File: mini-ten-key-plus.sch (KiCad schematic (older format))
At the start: 45 parts, among them SW0 SW_Push, U0 ProMicro

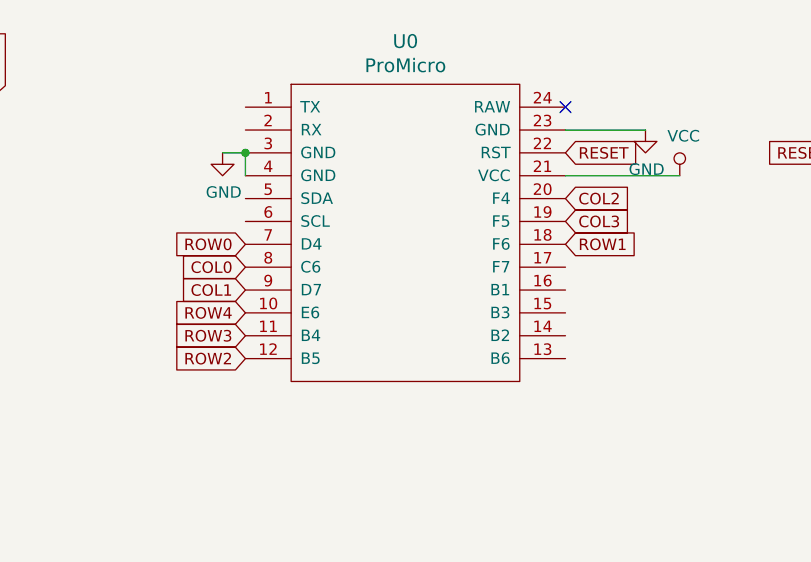
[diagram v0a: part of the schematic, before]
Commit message: Flipped Pro Micro and redid rows/cols
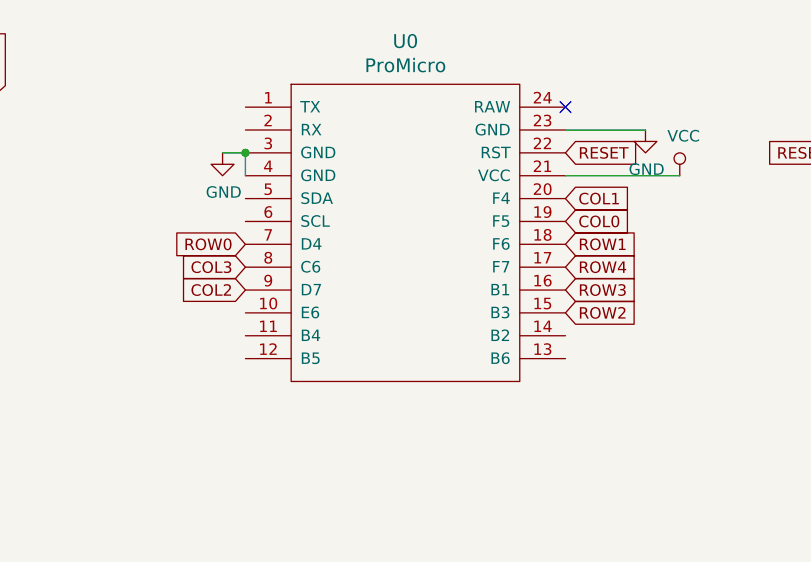
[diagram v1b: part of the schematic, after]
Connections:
- net COL0: now also U0.19 (F5); no longer U0.8 (C6)
- net COL1: now also U0.20 (F4); no longer U0.9 (D7)
- net COL2: now also U0.9 (D7); no longer U0.20 (F4)
- net COL3: now also U0.8 (C6); no longer U0.19 (F5)
- net ROW2: now also U0.15 (B3); no longer U0.12 (B5)
- net ROW3: now also U0.16 (B1); no longer U0.11 (B4)
- net ROW4: now also U0.17 (F7); no longer U0.10 (E6)
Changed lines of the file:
@@
 	1    0    0    -1
 $EndComp
+Text GLabel 3650 1550 0    50   Input ~ 0
+COL3
 Text GLabel 5050 1350 2    50   Input ~ 0
-COL3
-Text GLabel 3650 1550 0    50   Input ~ 0
 COL0
 Text GLabel 5050 1450 2    50   Input ~ 0
@@
 Text GLabel 3650 1450 0    50   Input ~ 0
 ROW0
-Text GLabel 3650 1950 0    50   Input ~ 0
+Text GLabel 5050 1750 2    50   Input ~ 0
 ROW2
-Text GLabel 3650 1750 0    50   Input ~ 0
+Text GLabel 5050 1550 2    50   Input ~ 0
 ROW4
-Text GLabel 3650 1850 0    50   Input ~ 0
+Text GLabel 5050 1650 2    50   Input ~ 0
 ROW3
+Text GLabel 5050 1250 2    50   Input ~ 0
+COL1
 Text GLabel 3650 1650 0    50   Input ~ 0
-COL1
-Text GLabel 5050 1250 2    50   Input ~ 0
 COL2
 $EndSCHEMATC

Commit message: General routing
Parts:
- added H0, H1, H2, H3, H4: MountingHole_Pad, mini-general-tweaks:MountingHole_2.2mm_M2_Pad_tweaked, symbol Mechanical:MountingHole_Pad
- MX21: footprint mini-MX-Tweaks:MXOnly-2U-NoLED_tweak -> mini-MX-Tweaks:MXOnly-2U-NoLED_FLIPPED_tweak
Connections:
- net GND: now also H0.1, H1.1, H2.1, H3.1, H4.1
- net ROW1: now also U0.16 (B1); no longer U0.18 (F6)
- net ROW2: now also U0.12 (B5); no longer U0.15 (B3)
- net ROW3: now also U0.11 (B4); no longer U0.16 (B1)
- net ROW4: now also U0.10 (E6); no longer U0.17 (F7)
- no-connect marks 1 -> 7
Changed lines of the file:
@@
 F 0 "MX21" H 1324 3973 60  0000 C CNN
 F 1 "MX-NoLED" H 1324 3899 20  0000 C CNN
-F 2 "mini-MX-Tweaks:MXOnly-2U-NoLED_tweak" H 725 3725 60  0001 C CNN
+F 2 "mini-MX-Tweaks:MXOnly-2U-NoLED_FLIPPED_tweak" H 725 3725 60  0001 C CNN
 F 3 "" H 725 3725 60  0001 C CNN
 	1    1350 3750
@@
 Text GLabel 5050 1350 2    50   Input ~ 0
 COL0
-Text GLabel 5050 1450 2    50   Input ~ 0
+Text GLabel 5050 1650 2    50   Input ~ 0
 ROW1
 Text GLabel 3650 1450 0    50   Input ~ 0
 ROW0
-Text GLabel 5050 1750 2    50   Input ~ 0
+Text GLabel 3650 1950 0    50   Input ~ 0
 ROW2
-Text GLabel 5050 1550 2    50   Input ~ 0
+Text GLabel 3650 1750 0    50   Input ~ 0
 ROW4
-Text GLabel 5050 1650 2    50   Input ~ 0
+Text GLabel 3650 1850 0    50   Input ~ 0
 ROW3
 Text GLabel 5050 1250 2    50   Input ~ 0
@@
 Text GLabel 3650 1650 0    50   Input ~ 0
 COL2
+NoConn ~ 3650 850
+NoConn ~ 3650 950
+NoConn ~ 3650 1250
+NoConn ~ 3650 1350
+NoConn ~ 5050 1850
+NoConn ~ 5050 1950
+$Comp
+L Mechanical:MountingHole_Pad H0
+U 1 1 617941C0
+P 3650 2550
+F 0 "H0" H 3750 2599 50  0000 L CNN
+F 1 "MountingHole_Pad" H 3750 2508 50  0000 L CNN
+F 2 "mini-general-tweaks:MountingHole_2.2mm_M2_Pad_tweaked" H 3650 2550 50  0001 C CNN
+F 3 "~" H 3650 2550 50  0001 C CNN
+	1    3650 2550
+	1    0    0    -1
+$EndComp
+$Comp
+L Mechanical:MountingHole_Pad H1
+U 1 1 61795197
+P 3650 2850
+F 0 "H1" H 3750 2899 50  0000 L CNN
+F 1 "MountingHole_Pad" H 3750 2808 50  0000 L CNN
+F 2 "mini-general-tweaks:MountingHole_2.2mm_M2_Pad_tweaked" H 3650 2850 50  0001 C CNN
+F 3 "~" H 3650 2850 50  0001 C CNN
+	1    3650 2850
+	1    0    0    -1
+$EndComp
+$Comp
+L Mechanical:MountingHole_Pad H2
+U 1 1 6179748B
+P 3650 3150
+F 0 "H2" H 3750 3199 50  0000 L CNN
+F 1 "MountingHole_Pad" H 3750 3108 50  0000 L CNN
+F 2 "mini-general-tweaks:MountingHole_2.2mm_M2_Pad_tweaked" H 3650 3150 50  0001 C CNN
+F 3 "~" H 3650 3150 50  0001 C CNN
+	1    3650 3150
+	1    0    0    -1
+$EndComp
+$Comp
+L Mechanical:MountingHole_Pad H3
+U 1 1 617998EF
+P 3650 3450
+F 0 "H3" H 3750 3499 50  0000 L CNN
+F 1 "MountingHole_Pad" H 3750 3408 50  0000 L CNN
+F 2 "mini-general-tweaks:MountingHole_2.2mm_M2_Pad_tweaked" H 3650 3450 50  0001 C CNN
+F 3 "~" H 3650 3450 50  0001 C CNN
+	1    3650 3450
+	1    0    0    -1
+$EndComp
+Wire Wire Line
+	3650 2650 3500 2650
+Wire Wire Line
+	3500 2650 3500 2950
+Wire Wire Line
+	3650 3550 3500 3550
+Wire Wire Line
+	3650 3250 3500 3250
+Connection ~ 3500 3250
+Wire Wire Line
+	3500 3250 3500 3550
+Wire Wire Line
+	3650 2950 3500 2950
+Connection ~ 3500 2950
+Wire Wire Line
+	3500 2950 3500 3250
+$Comp
+L power:GND #PWR0105
+U 1 1 617A50D9
+P 3500 3850
+F 0 "#PWR0105" H 3500 3600 50  0001 C CNN
+F 1 "GND" H 3505 3677 50  0000 C CNN
+F 2 "" H 3500 3850 50  0001 C CNN
+F 3 "" H 3500 3850 50  0001 C CNN
+	1    3500 3850
+	1    0    0    -1
+$EndComp
+$Comp
+L Mechanical:MountingHole_Pad H4
+U 1 1 617BCB5D
+P 3650 3750
+F 0 "H4" H 3750 3799 50  0000 L CNN
+F 1 "MountingHole_Pad" H 3750 3708 50  0000 L CNN
+F 2 "mini-general-tweaks:MountingHole_2.2mm_M2_Pad_tweaked" H 3650 3750 50  0001 C CNN
+F 3 "~" H 3650 3750 50  0001 C CNN
+	1    3650 3750
+	1    0    0    -1
+$EndComp
+Wire Wire Line
+	3500 3550 3500 3850
+Wire Wire Line
+	3500 3850 3650 3850
+Connection ~ 3500 3550
+Connection ~ 3500 3850
 $EndSCHEMATC

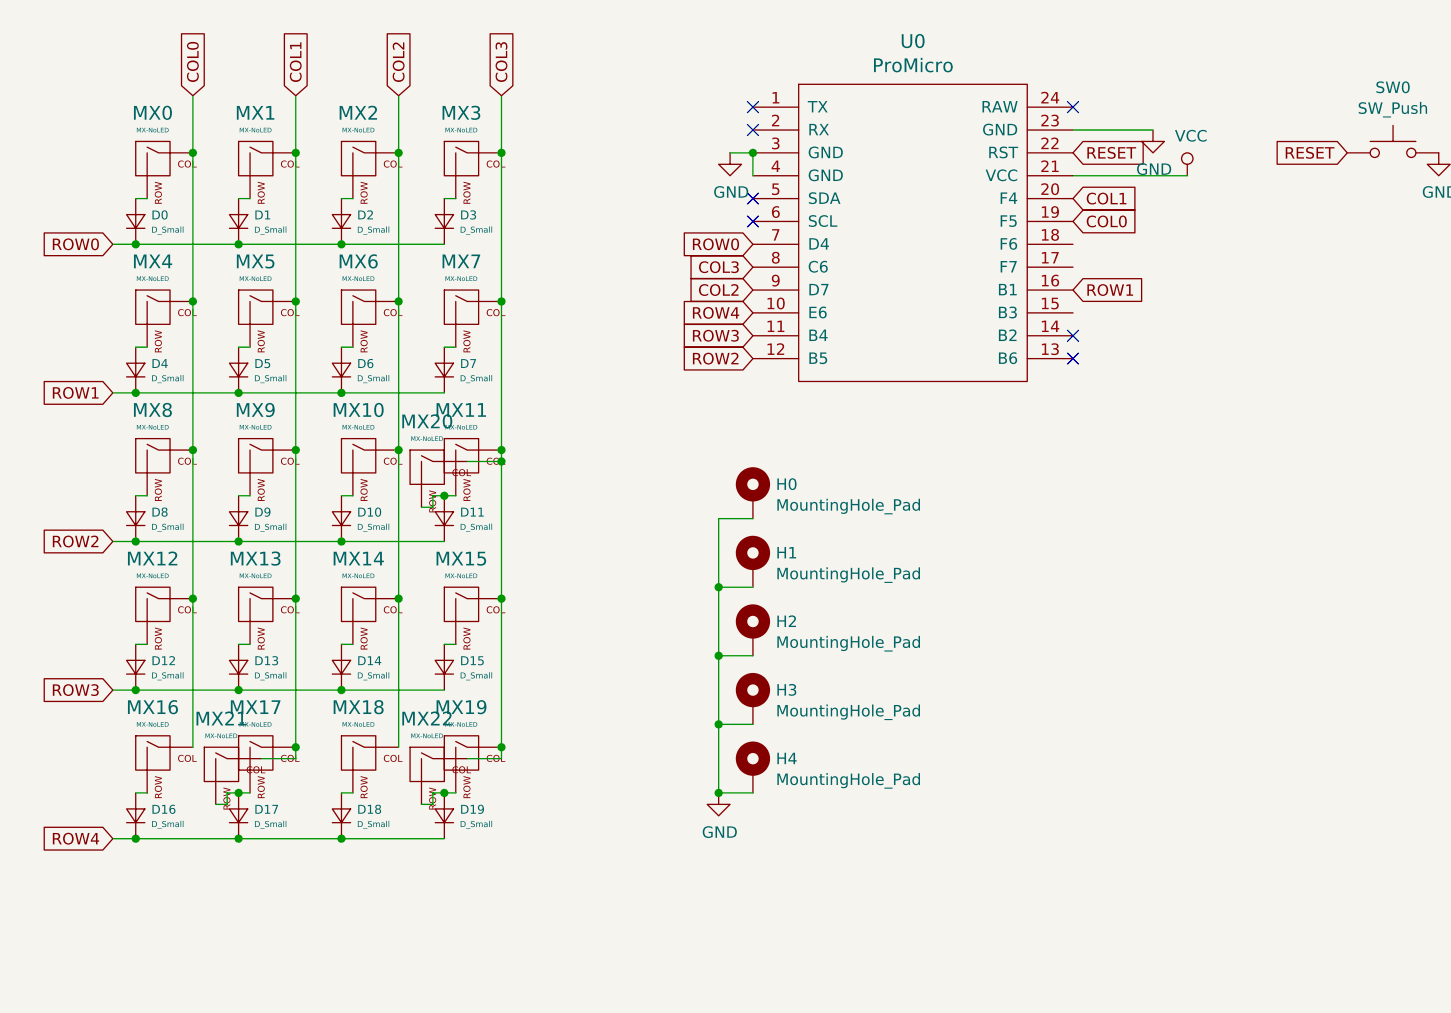
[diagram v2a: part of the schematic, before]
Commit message: Added extra column of keys on the left side
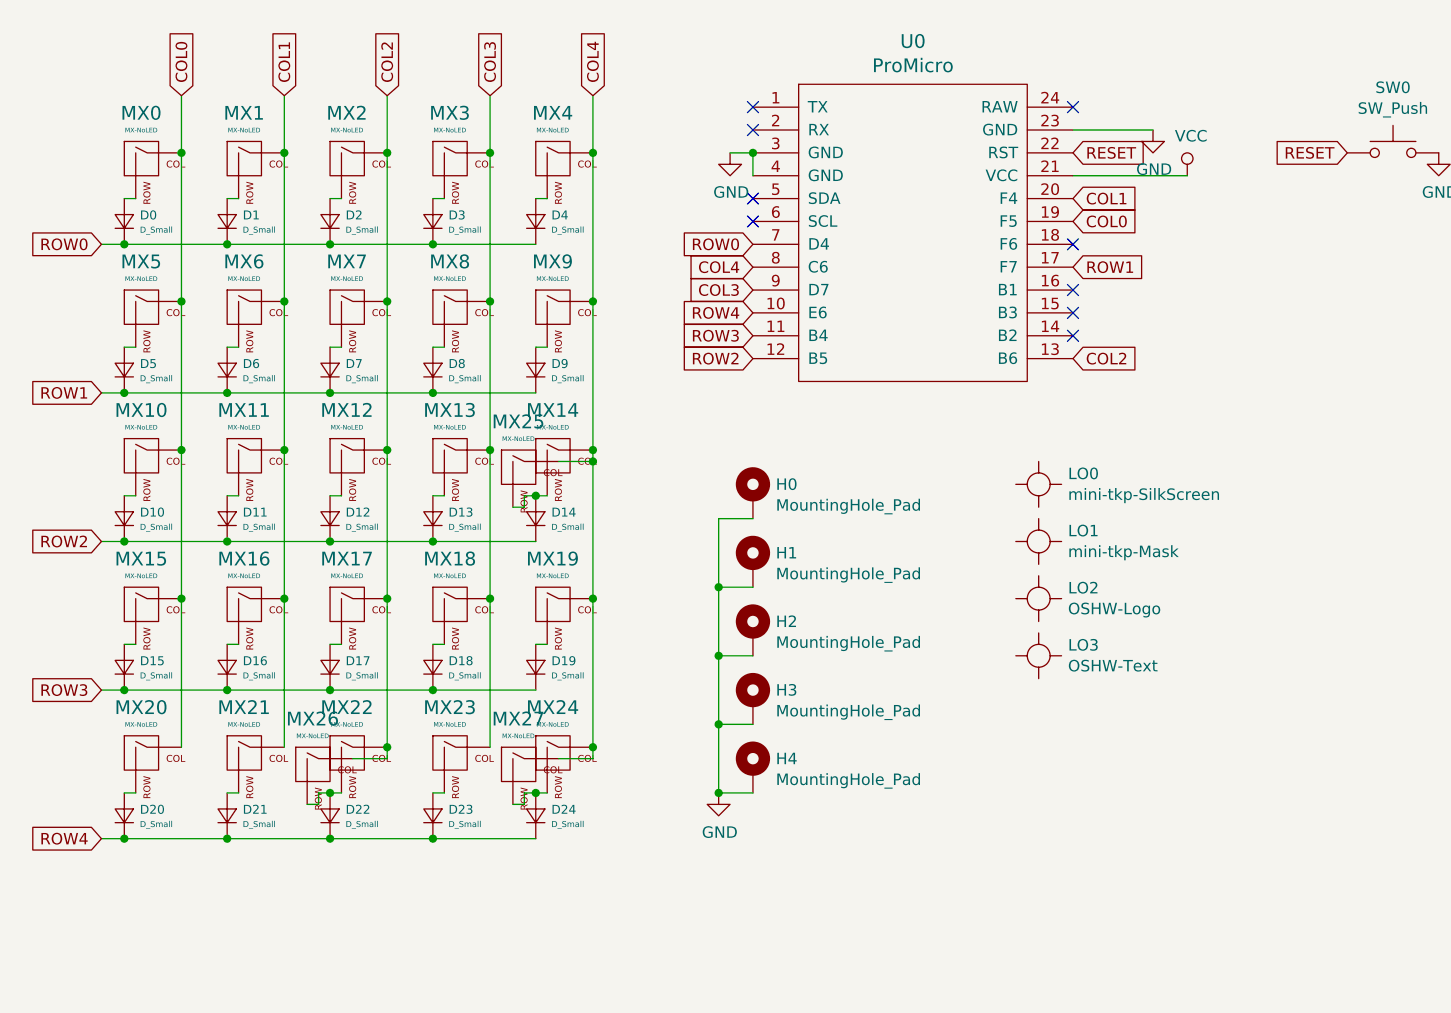
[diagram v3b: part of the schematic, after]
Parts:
- added D0, D10, D15, D20, D5: D_Small, mini-general-tweaks:D_SOD123_axial-dual, symbol Device:D_Small
- added LO0: mini-tkp-SilkScreen, mini-Logos:eLiXiVy-rev1.1-SilkScreen, symbol mini_random_library:Logo
- added LO1: mini-tkp-Mask, mini-Logos:eLiXiVy-rev1.1-Mask, symbol mini_random_library:Logo
- added LO2: OSHW-Logo, mini-Logos:OSHW-Logo, symbol mini_random_library:Logo
- added LO3: OSHW-Text, mini-Logos:OSHW-Text, symbol mini_random_library:Logo
- added MX0, MX10, MX15, MX20, MX5: MX-NoLED, mini-MX-Tweaks:MXOnly-1U-NoLED_tweak, symbol MX_Alps_Hybrid:MX-NoLED
- renumbered D0 to D1, D8 to D11, D9 to D12, D10 to D13, D11 to D14, D12 to D16, D13 to D17, D14 to D18, D15 to D19, D1 to D2, D16 to D21, D17 to D22, D18 to D23, D19 to D24, D2 to D3, D3 to D4, D4 to D6, D5 to D7, D6 to D8, D7 to D9, MX0 to MX1, MX8 to MX11, MX9 to MX12, MX10 to MX13, MX11 to MX14, MX12 to MX16, MX13 to MX17, MX14 to MX18, MX15 to MX19, MX1 to MX2, MX16 to MX21, MX17 to MX22, MX18 to MX23, MX19 to MX24, MX20 to MX25, MX21 to MX26, MX22 to MX27, MX2 to MX3, MX3 to MX4, MX4 to MX6, MX5 to MX7, MX6 to MX8, MX7 to MX9
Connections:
- net COL0: now also MX0.1 (COL), MX10.1 (COL), MX15.1 (COL), MX20.1 (COL), MX5.1 (COL); no longer MX1.1 (COL), MX11.1 (COL), MX16.1 (COL), MX21.1 (COL), MX6.1 (COL)
- net COL1: now also MX1.1 (COL), MX11.1 (COL), MX16.1 (COL), MX21.1 (COL), MX6.1 (COL); no longer MX12.1 (COL), MX17.1 (COL), MX2.1 (COL), MX22.1 (COL), MX26.1 (COL), MX7.1 (COL)
- net COL2: now also MX12.1 (COL), MX17.1 (COL), MX2.1 (COL), MX22.1 (COL), MX26.1 (COL), MX7.1 (COL), U0.13 (B6); no longer MX13.1 (COL), MX18.1 (COL), MX23.1 (COL), MX3.1 (COL), MX8.1 (COL), U0.9 (D7)
- net COL3: now also MX13.1 (COL), MX18.1 (COL), MX23.1 (COL), MX3.1 (COL), MX8.1 (COL), U0.9 (D7); no longer MX14.1 (COL), MX19.1 (COL), MX24.1 (COL), MX25.1 (COL), MX27.1 (COL), MX4.1 (COL), MX9.1 (COL), U0.8 (C6)
- net ROW0: now also D0.1 (K)
- net ROW1: now also U0.17 (F7), D5.1 (K); no longer U0.16 (B1)
- net ROW2: now also D10.1 (K)
- net ROW3: now also D15.1 (K)
- net ROW4: now also D20.1 (K)
- new net: D15.2 (A), MX15.2 (ROW)
- new net: D20.2 (A), MX20.2 (ROW)
- new net: D10.2 (A), MX10.2 (ROW)
- new net: D5.2 (A), MX5.2 (ROW)
- new net: D0.2 (A), MX0.2 (ROW)
- new net COL4: MX14.1 (COL), MX19.1 (COL), MX24.1 (COL), MX25.1 (COL), MX27.1 (COL), MX4.1 (COL), MX9.1 (COL), U0.8 (C6)
- no-connect marks 7 -> 9
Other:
- moved on the sheet: D1, D11, D12, D13, D14, D16, D17, D18, D19, D2, D21, D22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

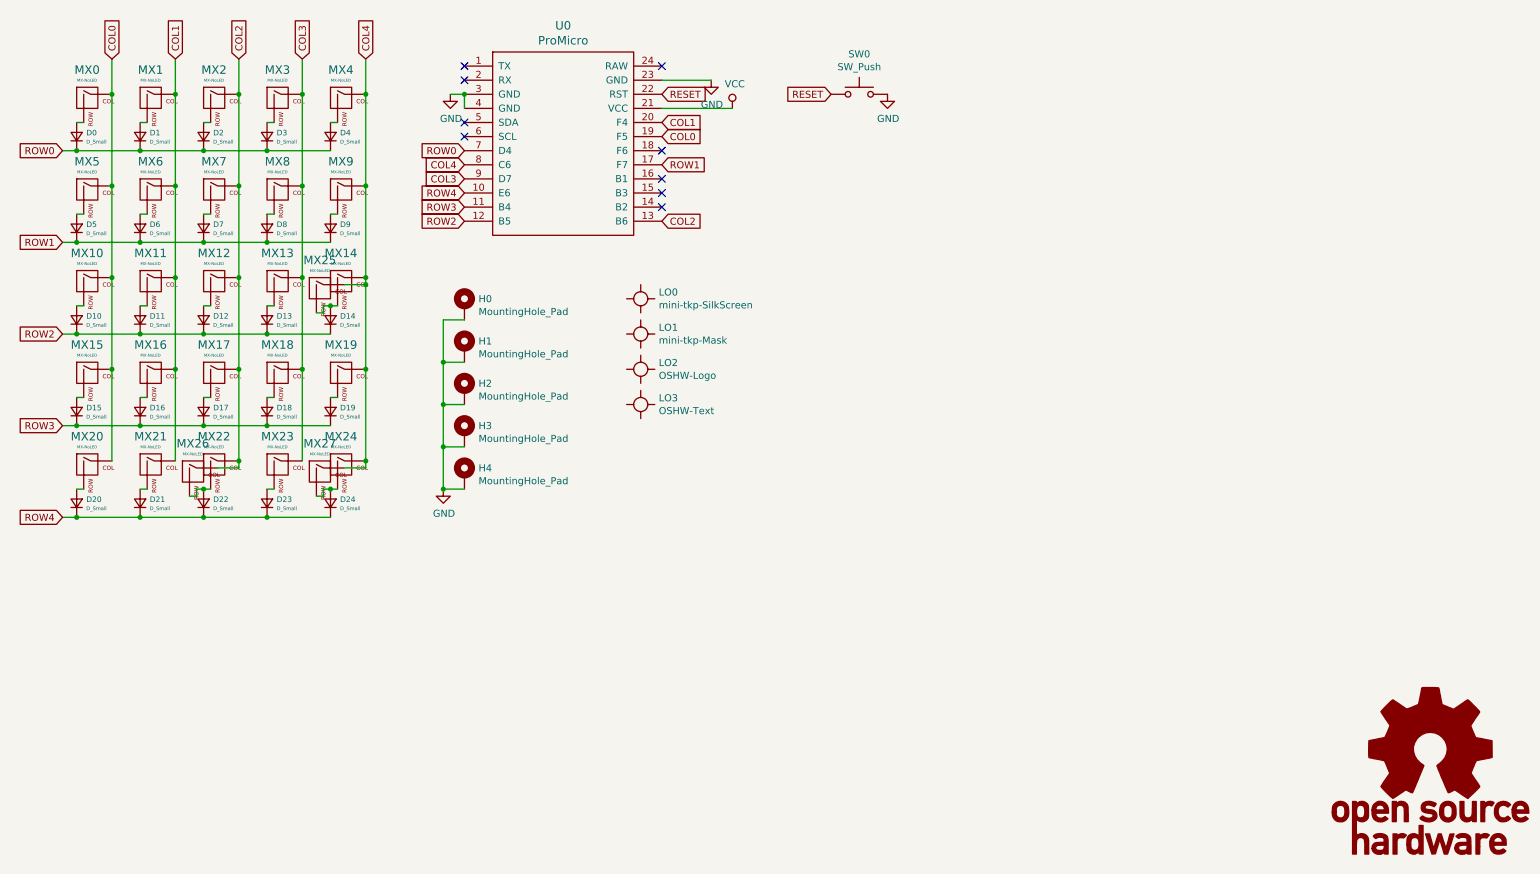
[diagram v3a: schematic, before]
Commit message: Cleaned up schematic
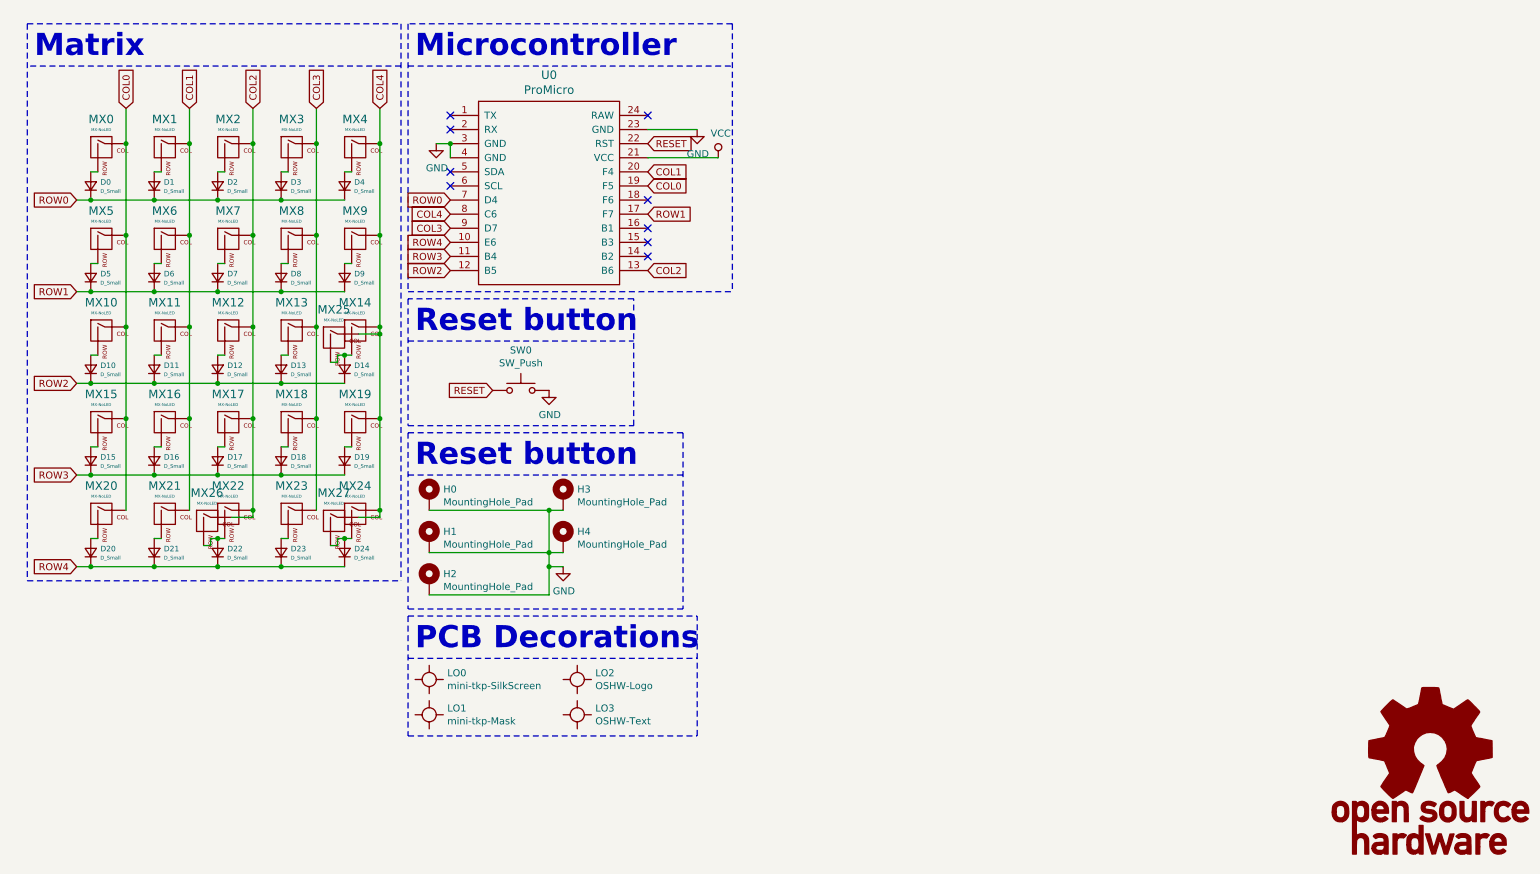
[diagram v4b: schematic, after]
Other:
- note added: "Matrix"
- note added: "Microcontroller"
- note added: "PCB Decorations"
- note added: "Reset button"
- moved on the sheet: D0, D1, D10, D11, D12, D13, D14, D15, D16, D17, D18, D19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
